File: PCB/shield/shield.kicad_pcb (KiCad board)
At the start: 2 copper layers, 99.6 x 80.1 mm, 20 parts, among them J1 QTR-8A, J10 ESP32_left_m, J11 ESP32_right_m, J13 Conn_01x06, J14 Domino, J15 Domino, J2 QMC5883L, J3 Servo, J4 Domino, J5 Joystick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

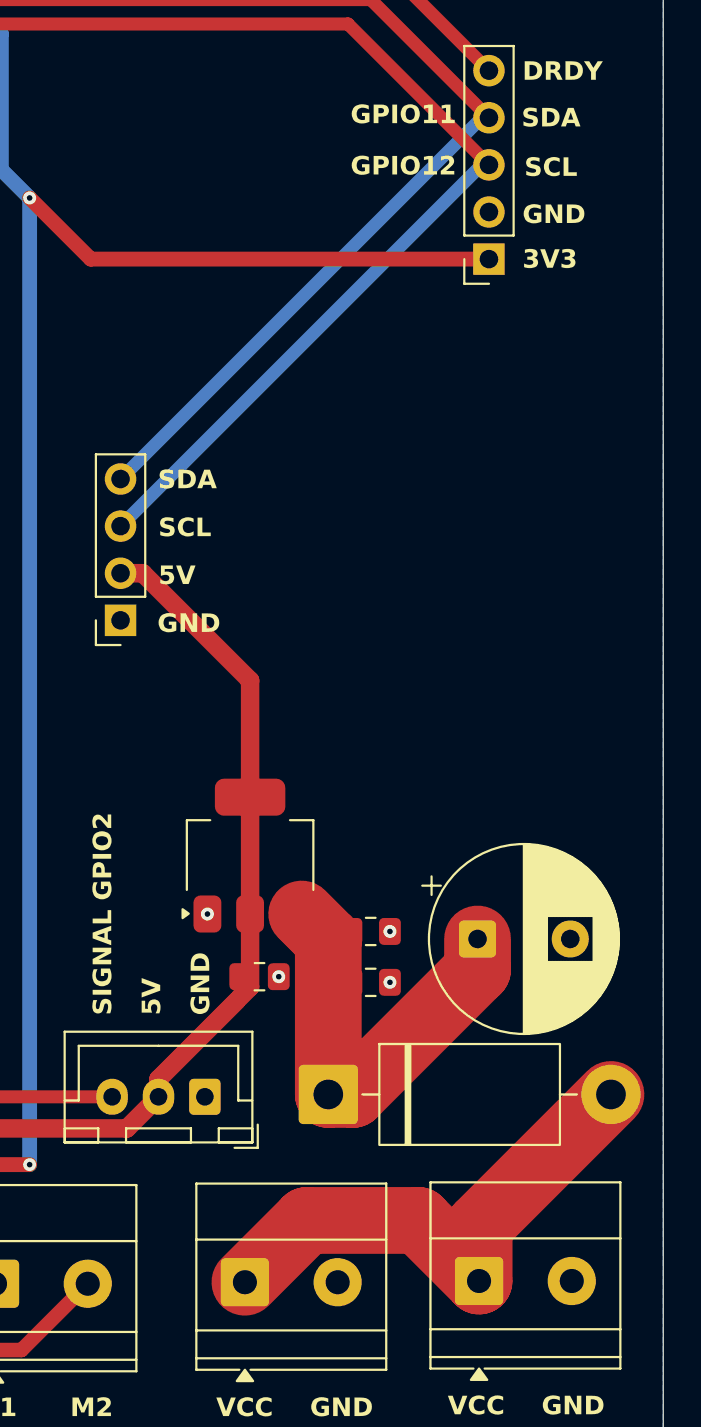
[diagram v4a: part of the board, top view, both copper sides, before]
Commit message: feat: change vcc trace width
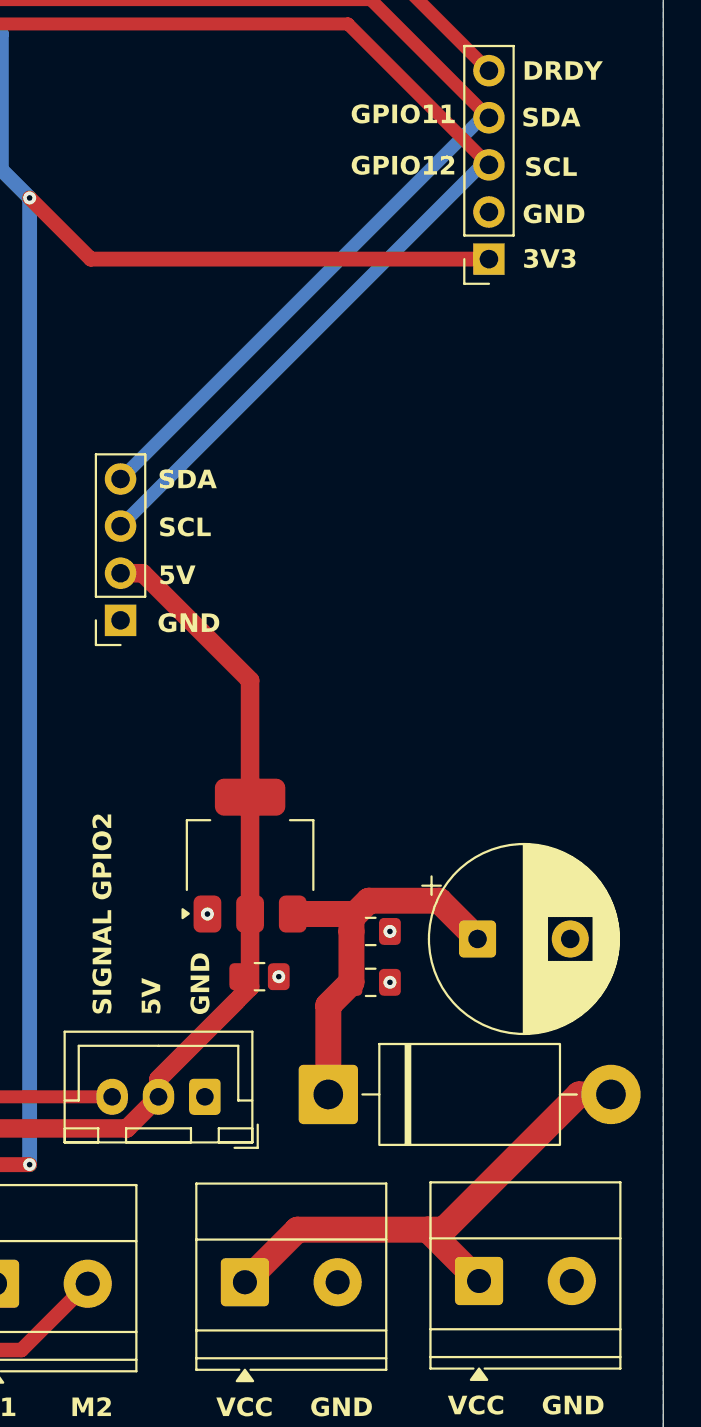
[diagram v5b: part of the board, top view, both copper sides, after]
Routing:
- net VCC: track 22.8 -> 21.3 mm
- net Net-(D1-A): track 28.4 -> 27.8 mm
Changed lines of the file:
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@@
+	)
+	(segment
+		(start 170.1219 118.7454)
+		(end 170.3363 118.9598)
+		(width 1.4)
+		(layer "F.Cu")
+		(net 1)
+	)
+	(segment
+		(start 169.0878 123.6765)
+		(end 170.3363 122.428)
+		(width 1.4)
+		(layer "F.Cu")
+		(net 1)
+	)
+	(segment
+		(start 170.3363 122.428)
+		(end 170.3363 119.6848)
+		(width 1.4)
+		(layer "F.Cu")
+		(net 1)
+	)
+	(segment
+		(start 167.1714 118.7454)
+		(end 170.1219 118.7454)
+		(width 1.4)
+		(layer "F.Cu")
+		(net 1)
+	)
+	(segment
+		(start 171.2673 118.0288)
+		(end 170.3363 118.9598)
+		(width 1.4)
+		(layer "F.Cu")
+		(net 1)
+	)
+	(segment
+		(start 175.071723 118.0288)
+		(end 171.2673 118.0288)
+		(width 1.4)
+		(layer "F.Cu")
+		(net 1)
 	)
 	(segment
 		(start 169.0878 128.4732)
-		(end 169.0878 120.1808)
-		(width 3.6)
+		(end 169.0878 123.6765)
+		(width 1.4)
 		(layer "F.Cu")
 		(net 1)
@@
 	(segment
 		(start 177.134123 120.0912)
-		(end 177.134123 121.750425)
-		(width 3.6)
+		(end 175.071723 118.0288)
+		(width 1.4)
 		(layer "F.Cu")
 		(net 1)
 	)
 	(segment
-		(start 169.0878 120.1808)
-		(end 167.6524 118.7454)
-		(width 3.6)
-		(layer "F.Cu")
-		(net 1)
-	)
-	(segment
-		(start 177.134123 121.750425)
-		(end 170.411348 128.4732)
-		(width 3.6)
-		(layer "F.Cu")
-		(net 1)
-	)
-	(segment
-		(start 170.411348 128.4732)
-		(end 169.0878 128.4732)
-		(width 3.6)
+		(start 170.3363 118.9598)
+		(end 170.3363 119.6848)
+		(width 1.4)
 		(layer "F.Cu")
 		(net 1)
@@
 	)
 	(segment
-		(start 177.3632 78.3544)
-		(end 177.7496 78.3544)
-		(width 0.7)
-		(layer "B.Cu")
-		(net 13)
-	)
-	(segment
 		(start 157.8868 97.8308)
 		(end 177.3632 78.3544)
@@
 	)
 	(segment
-		(start 177.3632 75.8144)
-		(end 177.7496 75.8144)
-		(width 0.7)
-		(layer "B.Cu")
-		(net 15)
-	)
-	(segment
 		(start 157.8868 95.2908)
 		(end 177.3632 75.8144)
@@
 	)
 	(segment
-		(start 164.8714 106.153319)
-		(end 159.088881 100.3708)
-		(width 1)
-		(layer "F.Cu")
-		(net 20)
-	)
-	(segment
 		(start 129.087 130.3062)
 		(end 125.6538 126.873)
@@
 	)
 	(segment
-		(start 164.8714 112.4454)
-		(end 164.8714 106.153319)
+		(start 164.8714 106.153319)
+		(end 164.8714 112.4454)
 		(width 1)
 		(layer "F.Cu")
@@
 	)
 	(segment
-		(start 159.088881 100.3708)
-		(end 157.8868 100.3708)
+		(start 157.8868 100.3708)
+		(end 159.088881 100.3708)
 		(width 1)
 		(layer "F.Cu")
@@
 	)
 	(segment
+		(start 159.088881 100.3708)
+		(end 164.8714 106.153319)
+		(width 1)
+		(layer "F.Cu")
+		(net 20)
+	)
+	(segment
 		(start 159.933 127.6419)
 		(end 159.933 128.6002)
@@
 	)
 	(segment
-		(start 177.2158 135.5852)
+		(start 175.3108 135.763)
+		(end 174.4472 135.763)
+		(width 1.4)
+		(layer "F.Cu")
+		(net 46)
+	)
+	(segment
+		(start 184.3278 128.4732)
+		(end 182.6006 128.4732)
+		(width 1.4)
+		(layer "F.Cu")
+		(net 46)
+	)
+	(segment
+		(start 182.6006 128.4732)
+		(end 175.3108 135.763)
+		(width 1.4)
+		(layer "F.Cu")
+		(net 46)
+	)
+	(segment
+		(start 174.4472 135.763)
 		(end 177.2158 138.5316)
-		(width 3.6)
+		(width 1.4)
 		(layer "F.Cu")
 		(net 46)
 	)
 	(segment
-		(start 167.923 135.2662)
+		(start 167.4262 135.763)
 		(end 164.592 138.5972)
-		(width 3.6)
+		(width 1.4)
 		(layer "F.Cu")
 		(net 46)
 	)
 	(segment
-		(start 173.9504 135.2662)
-		(end 167.923 135.2662)
-		(width 3.6)
+		(start 174.4472 135.763)
+		(end 167.4262 135.763)
+		(width 1.4)
 		(layer "F.Cu")
 		(net 46)
-	)
-	(segment
-		(start 184.3278 128.4732)
-		(end 177.2158 135.5852)
-		(width 3.6)
-		(layer "F.Cu")
-		(net 46)
-	)
-	(segment
-		(start 177.2158 138.5316)
-		(end 173.9504 135.2662)
-		(width 3.6)
-		(layer "F.Cu")
-		(net 46)

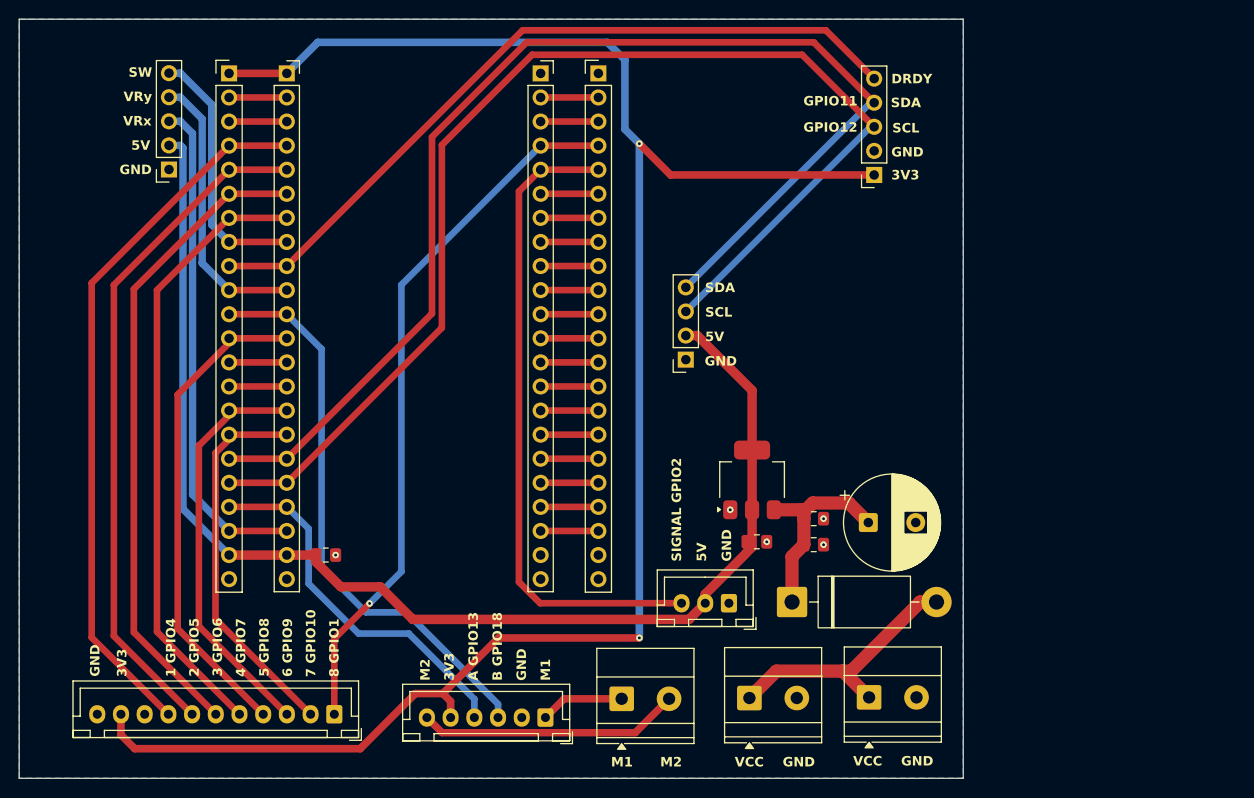
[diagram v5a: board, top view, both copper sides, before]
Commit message: feat: change AMS1117 to LM2596S
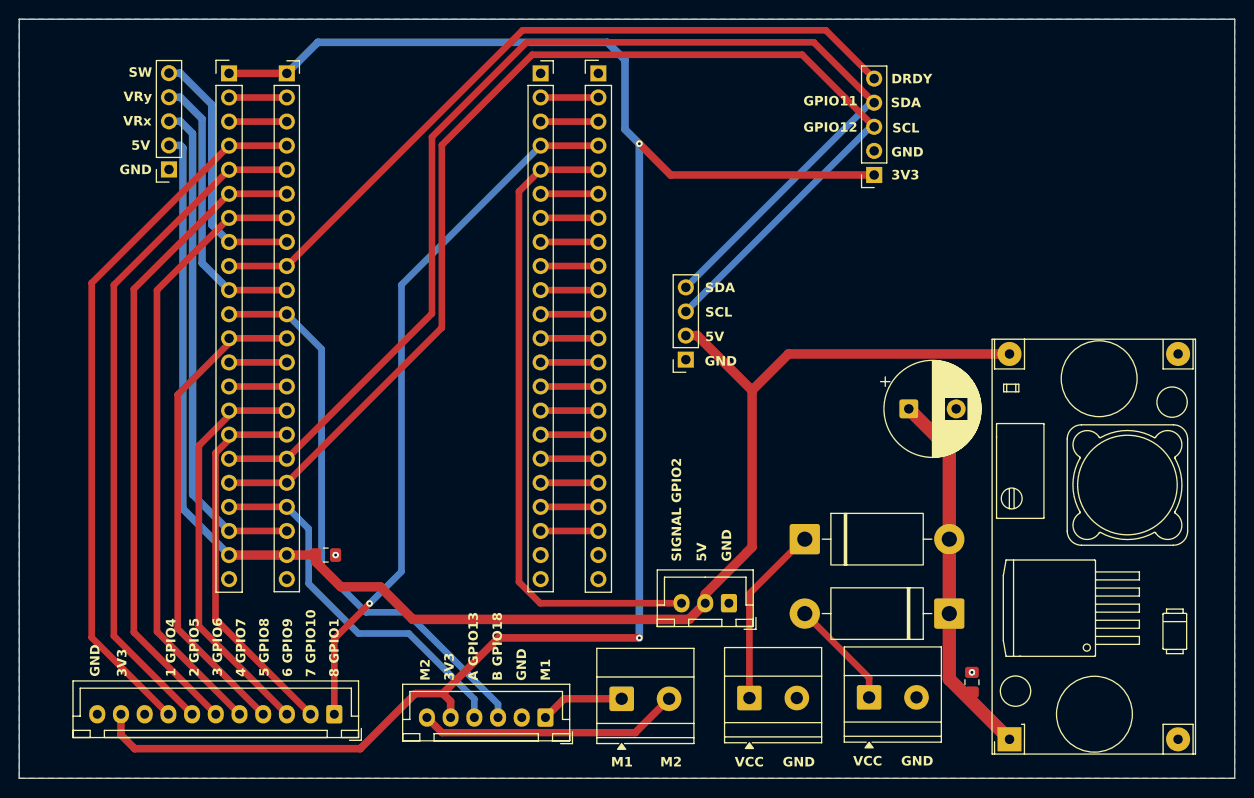
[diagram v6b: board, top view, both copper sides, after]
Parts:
- removed C2: 0.22uF, Capacitor_SMD:C_0805_2012Metric_Pad1.18x1.45mm_HandSolder
- removed C4: 10uF, Capacitor_SMD:C_0805_2012Metric_Pad1.18x1.45mm_HandSolder
- removed U2: AMS1117, Package_TO_SOT_SMD:SOT-223-3_TabPin2
- added D2: 1N5822, Diode_THT:D_DO-201AD_P15.24mm_Horizontal, F.Cu at (170.4, 121.8)
- added U1: YAAJ_DCDC_StepDown_LM2596, KiCad:YAAJ_DCDC_StepDown_LM2596, F.Cu at (192.0, 143.0)
- moved C3 22.1 mm to (188.1, 136.9), turned to 90 degrees
- moved D1 16.6 mm to (185.7, 129.7), turned to 180 degrees
- moved C1 12.7 mm to (181.4, 108.1)
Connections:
- J15 pad 1: Net-(D1-A) -> Net-(D2-K)
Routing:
- net +5V: track 134.3 -> 163.1 mm
- net Net-(D2-K): track 0.00 -> 19.3 mm
- net VCC: track 21.3 -> 39.2 mm
- net Net-(D1-A): track 27.8 -> 11.6 mm
- net GND: vias 5 -> 2
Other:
- board size 99.6 x 80.1 mm -> 128.2 x 80.1 mm

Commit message: wip: fixing multiple gpio traces
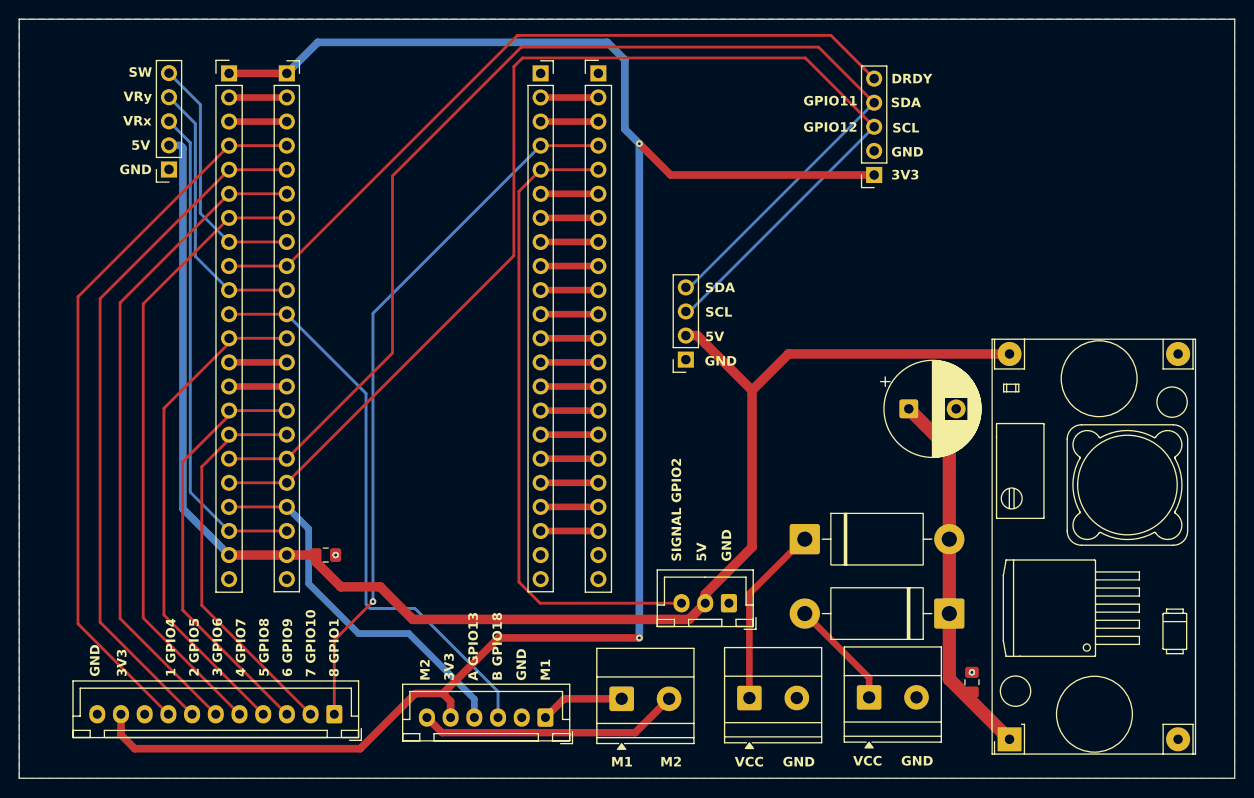
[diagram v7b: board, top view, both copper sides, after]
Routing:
- net /GPIO9: track 43.5 -> 44.9 mm
- net /GPIO7: track 65.2 -> 66.4 mm
- net /GPIO5: track 72.0 -> 73.2 mm
- net /GPIO4: track 75.4 -> 76.6 mm
- net /GPIO8: track 51.9 -> 53.1 mm
- net /GPIO10: track 40.5 -> 41.7 mm
- net /GPIO6: track 68.7 -> 69.9 mm
- net /GPIO15: track 27.2 -> 26.5 mm
- net /GPIO14: track 52.6 -> 51.9 mm
- net /GPIO17: track 29.8 -> 29.1 mm

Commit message: feat: change pcb trace width; change sensors input voltage
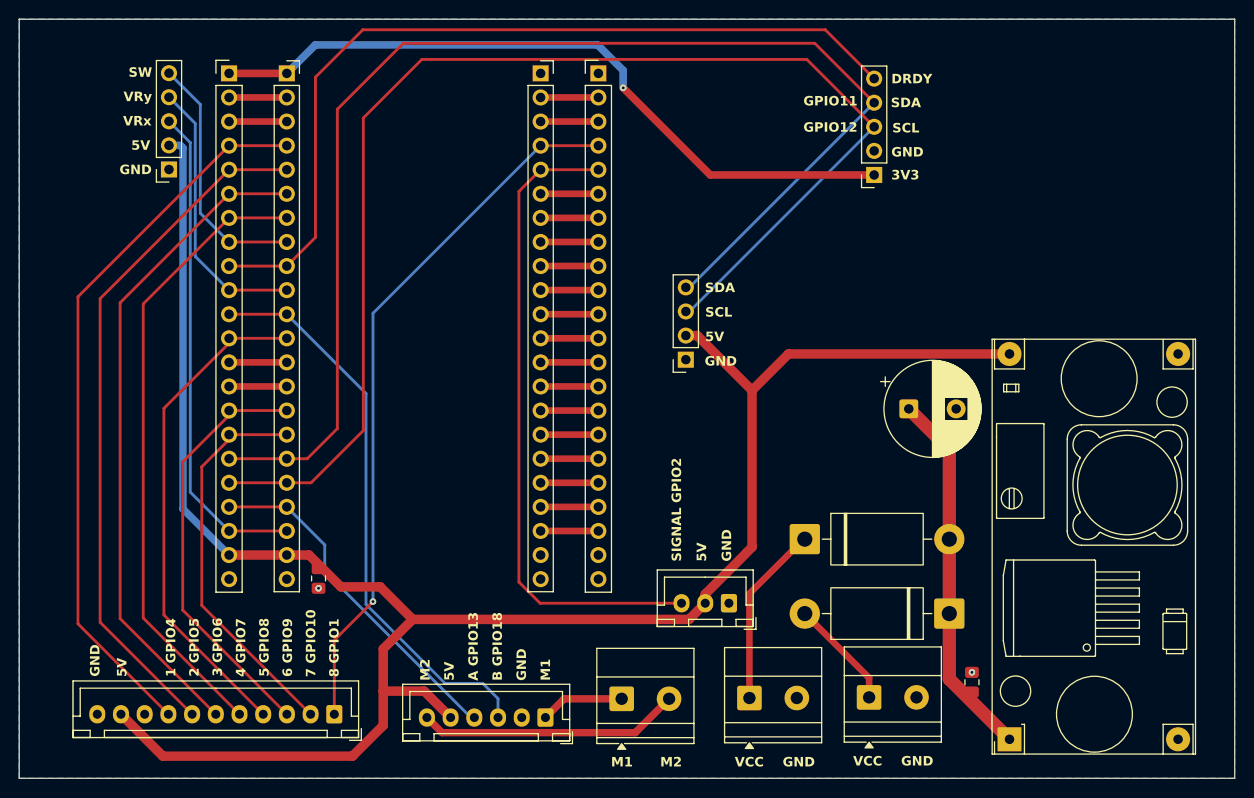
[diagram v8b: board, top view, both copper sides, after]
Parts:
- moved C5 2.58 mm to (119.2, 126.0), turned to -90 degrees
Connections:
- J1 pad 10: +3V3 -> +5V
- J13 pad 5: +3V3 -> +5V
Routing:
- net +3V3: track 196.8 -> 76.0 mm, vias 2 -> 1
- net +5V: track 163.1 -> 214.2 mm
- net /GPIO16: track 80.0 -> 90.4 mm
- net /GPIO11+SDA: track 127.3 -> 136.4 mm
- net /GPIO12+SCL: track 129.2 -> 136.7 mm
- net /GPIO13: track 39.6 -> 36.7 mm
